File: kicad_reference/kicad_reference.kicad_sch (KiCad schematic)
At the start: 1 part, among them U1 AMS1117-3.3

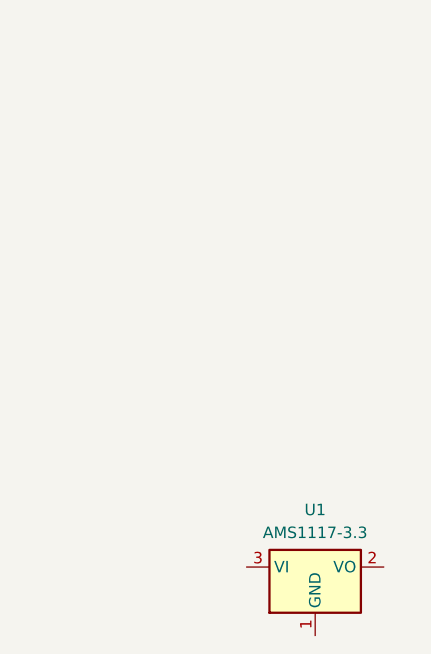
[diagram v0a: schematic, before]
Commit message: Fix multi-unit component support in Rust KiCad integration
Handles complex geometry naming for multi-unit components and extended symbols

🤖 Generated with Claude Code
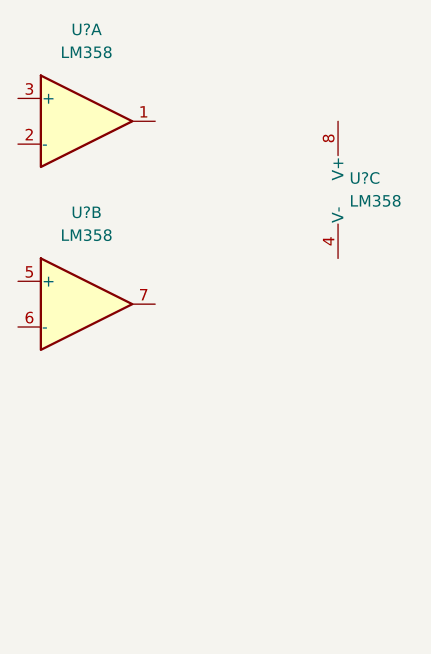
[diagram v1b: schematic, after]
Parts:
- removed U1: AMS1117-3.3, Package_TO_SOT_SMD:SOT-223-3_TabPin2, symbol Regulator_Linear:AMS1117-3.3
- added U? (x3): LM358, symbol Amplifier_Operational:LM358
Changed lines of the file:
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@@
 	(paper "A4")
 	(symbol
-		(lib_id "Regulator_Linear:AMS1117-3.3")
-		(at 135.89 96.52 0)
+		(lib_id "Amplifier_Operational:LM358")
+		(at 110.49 67.31 0)
+		(unit 2)
+		(exclude_from_sim no)
+		(in_bom yes)
+		(on_board yes)
+		(dnp no)
+		(fields_autoplaced yes)
+		(property "Reference" "U?"
+			(at 110.49 57.15 0)
+			(effects
+				(font
+					(size 1.27 1.27)
+				)
+			)
+		)
+		(property "Value" "LM358"
+			(at 110.49 59.69 0)
+			(effects
+				(font
+					(size 1.27 1.27)
+				)
+			)
+		)
+		(property "Footprint" ""
+			(at 110.49 67.31 0)
+			(effects
+				(font
+					(size 1.27 1.27)
+				)
+				(hide yes)
+			)
+		)
+		(property "Datasheet" "http://www.ti.com/lit/ds/symlink/lm2904-n.pdf"
+			(at 110.49 67.31 0)
+			(effects
+				(font
+					(size 1.27 1.27)
+				)
+				(hide yes)
+			)
+		)
+		(property "Description" "Low-Power, Dual Operational Amplifiers, DIP-8/SOIC-8/TO-99-8"
+			(at 110.49 67.31 0)
+			(effects
+				(font
+					(size 1.27 1.27)
+				)
+				(hide yes)
+			)
+		)
+		(pin "3"
+		)
+		(pin "8"
+		)
+		(pin "4"
+		)
+		(pin "2"
+		)
+		(pin "1"
+		)
+		(pin "5"
+		)
+		(pin "6"
+		)
+		(pin "7"
+		)
+		(instances
+			(project ""
+				(path "/5f0ac341-7bbd-4a3f-be5f-8ffd62126d0c"
+					(reference "U?")
+					(unit 2)
+				)
+			)
+		)
+	)
+	(symbol
+		(lib_id "Amplifier_Operational:LM358")
+		(at 140.97 54.61 0)
+		(unit 3)
+		(exclude_from_sim no)
+		(in_bom yes)
+		(on_board yes)
+		(dnp no)
+		(fields_autoplaced yes)
+		(property "Reference" "U?"
+			(at 139.7 53.3399 0)
+			(effects
+				(font
+					(size 1.27 1.27)
+				)
+				(justify left)
+			)
+		)
+		(property "Value" "LM358"
+			(at 139.7 55.8799 0)
+			(effects
+				(font
+					(size 1.27 1.27)
+				)
+				(justify left)
+			)
+		)
+		(property "Footprint" ""
+			(at 140.97 54.61 0)
+			(effects
+				(font
+					(size 1.27 1.27)
+				)
+				(hide yes)
+			)
+		)
+		(property "Datasheet" "http://www.ti.com/lit/ds/symlink/lm2904-n.pdf"
+			(at 140.97 54.61 0)
+			(effects
+				(font
+					(size 1.27 1.27)
+				)
+				(hide yes)
+			)
+		)
+		(property "Description" "Low-Power, Dual Operational Amplifiers, DIP-8/SOIC-8/TO-99-8"
+			(at 140.97 54.61 0)
+			(effects
+				(font
+					(size 1.27 1.27)
+				)
+				(hide yes)
+			)
+		)
+		(pin "3"
+		)
+		(pin "8"
+		)
+		(pin "4"
+		)
+		(pin "2"
+		)
+		(pin "1"
+		)
+		(pin "5"
+		)
+		(pin "6"
+		)
+		(pin "7"
+		)
+		(instances
+			(project ""
+				(path "/5f0ac341-7bbd-4a3f-be5f-8ffd62126d0c"
+					(reference "U?")
+					(unit 3)
+				)
+			)
+		)
+	)
+	(symbol
+		(lib_id "Amplifier_Operational:LM358")
+		(at 110.49 46.99 0)
 		(unit 1)
 		(exclude_from_sim no)
@@
 		(dnp no)
 		(fields_autoplaced yes)
-		(property "Reference" "U1"
-			(at 135.89 90.17 0)
-			(effects
-				(font
-					(size 1.27 1.27)
-				)
-			)
-		)
-		(property "Value" "AMS1117-3.3"
-			(at 135.89 92.71 0)
-			(effects
-				(font
-					(size 1.27 1.27)
-				)
-			)
-		)
-		(property "Footprint" "Package_TO_SOT_SMD:SOT-223-3_TabPin2"
-			(at 135.89 91.44 0)
-			(effects
-				(font
-					(size 1.27 1.27)
-				)
-				(hide yes)
-			)
-		)
-		(property "Datasheet" "http://www.advanced-monolithic.com/pdf/ds1117.pdf"
-			(at 138.43 102.87 0)
-			(effects
-				(font
-					(size 1.27 1.27)
-				)
-				(hide yes)
-			)
-		)
-		(property "Description" "1A Low Dropout regulator, positive, 3.3V fixed output, SOT-223"
-			(at 135.89 96.52 0)
-			(effects
-				(font
-					(size 1.27 1.27)
-				)
-				(hide yes)
-			)
+		(property "Reference" "U?"
+			(at 110.49 36.83 0)
+			(effects
+				(font
+					(size 1.27 1.27)
+				)
+			)
+		)
+		(property "Value" "LM358"
+			(at 110.49 39.37 0)
+			(effects
+				(font
+					(size 1.27 1.27)
+				)
+			)
+		)
+		(property "Footprint" ""
+			(at 110.49 46.99 0)
+			(effects
+				(font
+					(size 1.27 1.27)
+				)
+				(hide yes)
+			)
+		)
+		(property "Datasheet" "http://www.ti.com/lit/ds/symlink/lm2904-n.pdf"
+			(at 110.49 46.99 0)
+			(effects
+				(font
+					(size 1.27 1.27)
+				)
+				(hide yes)
+			)
+		)
+		(property "Description" "Low-Power, Dual Operational Amplifiers, DIP-8/SOIC-8/TO-99-8"
+			(at 110.49 46.99 0)
+			(effects
+				(font
+					(size 1.27 1.27)
+				)
+				(hide yes)
+			)
+		)
+		(pin "3"
+		)
+		(pin "8"
+		)
+		(pin "4"
+		)
+		(pin "2"
 		)
 		(pin "1"
 		)
-		(pin "2"
-		)
-		(pin "3"
+		(pin "5"
+		)
+		(pin "6"
+		)
+		(pin "7"
 		)
 		(instances
-			(project "kicad_reference"
+			(project ""
 				(path "/5f0ac341-7bbd-4a3f-be5f-8ffd62126d0c"
-					(reference "U1")
+					(reference "U?")
 					(unit 1)
 				)

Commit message: Add hierarchical label support and clean up test files
- Implemented add_hierarchical_label_to_schematic() function
- Moved example scripts to examples/kicad_generation/
- Removed temporary test files

🤖 Generated with Claude Code
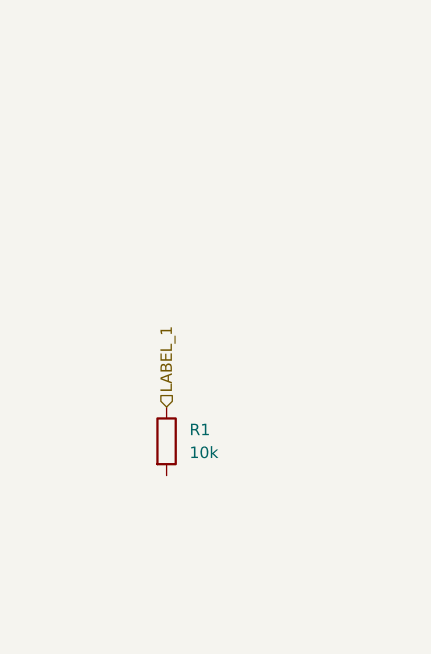
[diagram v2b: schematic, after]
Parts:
- removed U? (x3): LM358, symbol Amplifier_Operational:LM358
- added R1: 10k, Resistor_SMD:R_0603_1608Metric, symbol Device:R
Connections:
- new net LABEL_1: R1.1
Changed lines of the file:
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@@
 	(generator_version "9.0")
 	(paper "A4")
+	(hierarchical_label "LABEL_1"
+		(shape input)
+		(at 119.38 78.74 90)
+		(effects
+			(font
+				(size 1.27 1.27)
+			)
+			(justify left)
+		)
+	)
 	(symbol
-		(lib_id "Amplifier_Operational:LM358")
-		(at 110.49 67.31 0)
-		(unit 2)
+		(lib_id "Device:R")
+		(at 119.38 82.55 0)
+		(unit 1)
 		(exclude_from_sim no)
 		(in_bom yes)
@@
 		(dnp no)
 		(fields_autoplaced yes)
-		(property "Reference" "U?"
-			(at 110.49 57.15 0)
+		(property "Reference" "R1"
+			(at 121.92 81.2799 0)
 			(effects
 				(font
 					(size 1.27 1.27)
 				)
+				(justify left)
 			)
 		)
-		(property "Value" "LM358"
-			(at 110.49 59.69 0)
+		(property "Value" "10k"
+			(at 121.92 83.8199 0)
 			(effects
 				(font
 					(size 1.27 1.27)
 				)
+				(justify left)
 			)
 		)
-		(property "Footprint" ""
-			(at 110.49 67.31 0)
+		(property "Footprint" "Resistor_SMD:R_0603_1608Metric"
+			(at 117.602 82.55 90)
 			(effects
 				(font
@@
 			)
 		)
-		(property "Datasheet" "http://www.ti.com/lit/ds/symlink/lm2904-n.pdf"
-			(at 110.49 67.31 0)
+		(property "Datasheet" "~"
+			(at 119.38 82.55 0)
 			(effects
 				(font
@@
 			)
 		)
-		(property "Description" "Low-Power, Dual Operational Amplifiers, DIP-8/SOIC-8/TO-99-8"
-			(at 110.49 67.31 0)
+		(property "Description" "Resistor"
+			(at 119.38 82.55 0)
 			(effects
 				(font
@@
 			)
 		)
-		(pin "3"
-		)
-		(pin "8"
-		)
-		(pin "4"
+		(pin "1"
 		)
 		(pin "2"
 		)
-		(pin "1"
-		)
-		(pin "5"
-		)
-		(pin "6"
-		)
-		(pin "7"
-		)
 		(instances
-			(project ""
+			(project "kicad_reference"
 				(path "/5f0ac341-7bbd-4a3f-be5f-8ffd62126d0c"
-					(reference "U?")
-					(unit 2)
-				)
-			)
-		)
-	)
-	(symbol
-		(lib_id "Amplifier_Operational:LM358")
-		(at 140.97 54.61 0)
-		(unit 3)
-		(exclude_from_sim no)
-		(in_bom yes)
-		(on_board yes)
-		(dnp no)
-		(fields_autoplaced yes)
-		(property "Reference" "U?"
-			(at 139.7 53.3399 0)
-			(effects
-				(font
-					(size 1.27 1.27)
-				)
-				(justify left)
-			)
-		)
-		(property "Value" "LM358"
-			(at 139.7 55.8799 0)
-			(effects
-				(font
-					(size 1.27 1.27)
-				)
-				(justify left)
-			)
-		)
-		(property "Footprint" ""
-			(at 140.97 54.61 0)
-			(effects
-				(font
-					(size 1.27 1.27)
-				)
-				(hide yes)
-			)
-		)
-		(property "Datasheet" "http://www.ti.com/lit/ds/symlink/lm2904-n.pdf"
-			(at 140.97 54.61 0)
-			(effects
-				(font
-					(size 1.27 1.27)
-				)
-				(hide yes)
-			)
-		)
-		(property "Description" "Low-Power, Dual Operational Amplifiers, DIP-8/SOIC-8/TO-99-8"
-			(at 140.97 54.61 0)
-			(effects
-				(font
-					(size 1.27 1.27)
-				)
-				(hide yes)
-			)
-		)
-		(pin "3"
-		)
-		(pin "8"
-		)
-		(pin "4"
-		)
-		(pin "2"
-		)
-		(pin "1"
-		)
-		(pin "5"
-		)
-		(pin "6"
-		)
-		(pin "7"
-		)
-		(instances
-			(project ""
-				(path "/5f0ac341-7bbd-4a3f-be5f-8ffd62126d0c"
-					(reference "U?")
-					(unit 3)
-				)
-			)
-		)
-	)
-	(symbol
-		(lib_id "Amplifier_Operational:LM358")
-		(at 110.49 46.99 0)
-		(unit 1)
-		(exclude_from_sim no)
-		(in_bom yes)
-		(on_board yes)
-		(dnp no)
-		(fields_autoplaced yes)
-		(property "Reference" "U?"
-			(at 110.49 36.83 0)
-			(effects
-				(font
-					(size 1.27 1.27)
-				)
-			)
-		)
-		(property "Value" "LM358"
-			(at 110.49 39.37 0)
-			(effects
-				(font
-					(size 1.27 1.27)
-				)
-			)
-		)
-		(property "Footprint" ""
-			(at 110.49 46.99 0)
-			(effects
-				(font
-					(size 1.27 1.27)
-				)
-				(hide yes)
-			)
-		)
-		(property "Datasheet" "http://www.ti.com/lit/ds/symlink/lm2904-n.pdf"
-			(at 110.49 46.99 0)
-			(effects
-				(font
-					(size 1.27 1.27)
-				)
-				(hide yes)
-			)
-		)
-		(property "Description" "Low-Power, Dual Operational Amplifiers, DIP-8/SOIC-8/TO-99-8"
-			(at 110.49 46.99 0)
-			(effects
-				(font
-					(size 1.27 1.27)
-				)
-				(hide yes)
-			)
-		)
-		(pin "3"
-		)
-		(pin "8"
-		)
-		(pin "4"
-		)
-		(pin "2"
-		)
-		(pin "1"
-		)
-		(pin "5"
-		)
-		(pin "6"
-		)
-		(pin "7"
-		)
-		(instances
-			(project ""
-				(path "/5f0ac341-7bbd-4a3f-be5f-8ffd62126d0c"
-					(reference "U?")
+					(reference "R1")
 					(unit 1)
 				)
